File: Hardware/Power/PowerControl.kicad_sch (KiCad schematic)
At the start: 33 parts, among them Q10 BSS84, Q11 2N7002PW, Q12 2N7002PW, Q13 2N7002PW, Q14 Si7141DP, Q15 BSS84, Q16 Si7141DP, Q17 Si7141DP, Q18 Si7141DP, Q19 BSS84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

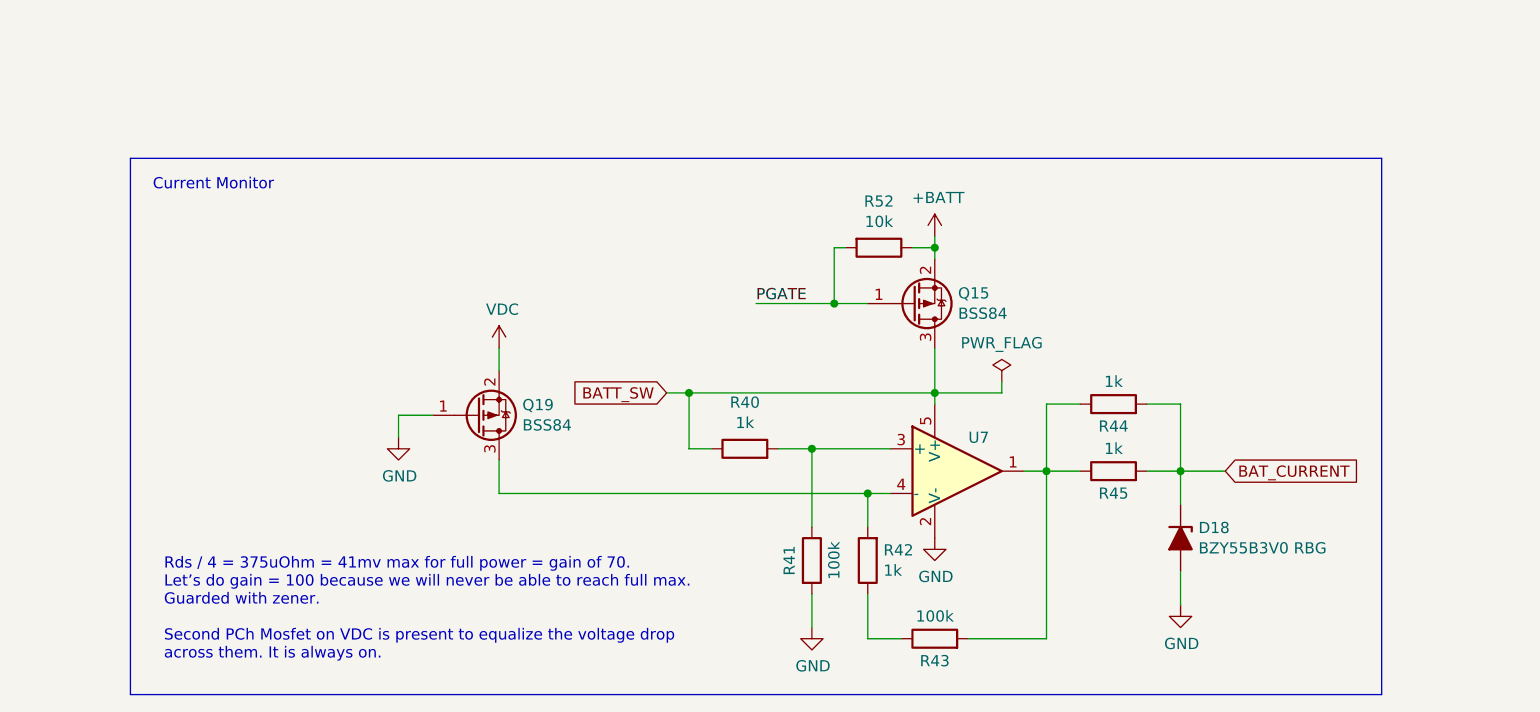
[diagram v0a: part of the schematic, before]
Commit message: Update to kicad 8
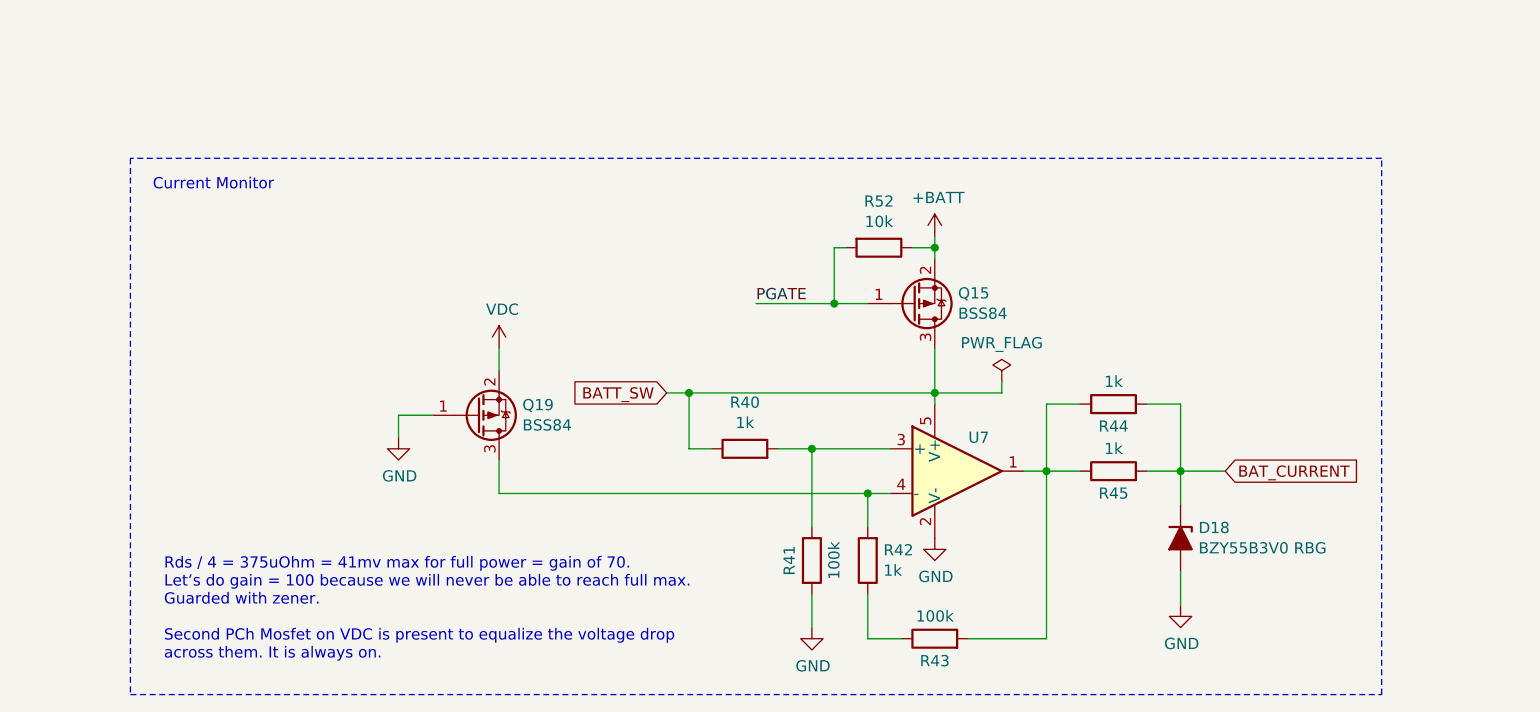
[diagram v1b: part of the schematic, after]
